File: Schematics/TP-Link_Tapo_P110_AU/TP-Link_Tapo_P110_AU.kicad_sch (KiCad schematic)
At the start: 28 parts, among them J1 KB-6160 Daughterboard, Q2 MMBT3904, Q3 MMBT3904, U1 SY22841, U7 BL0937

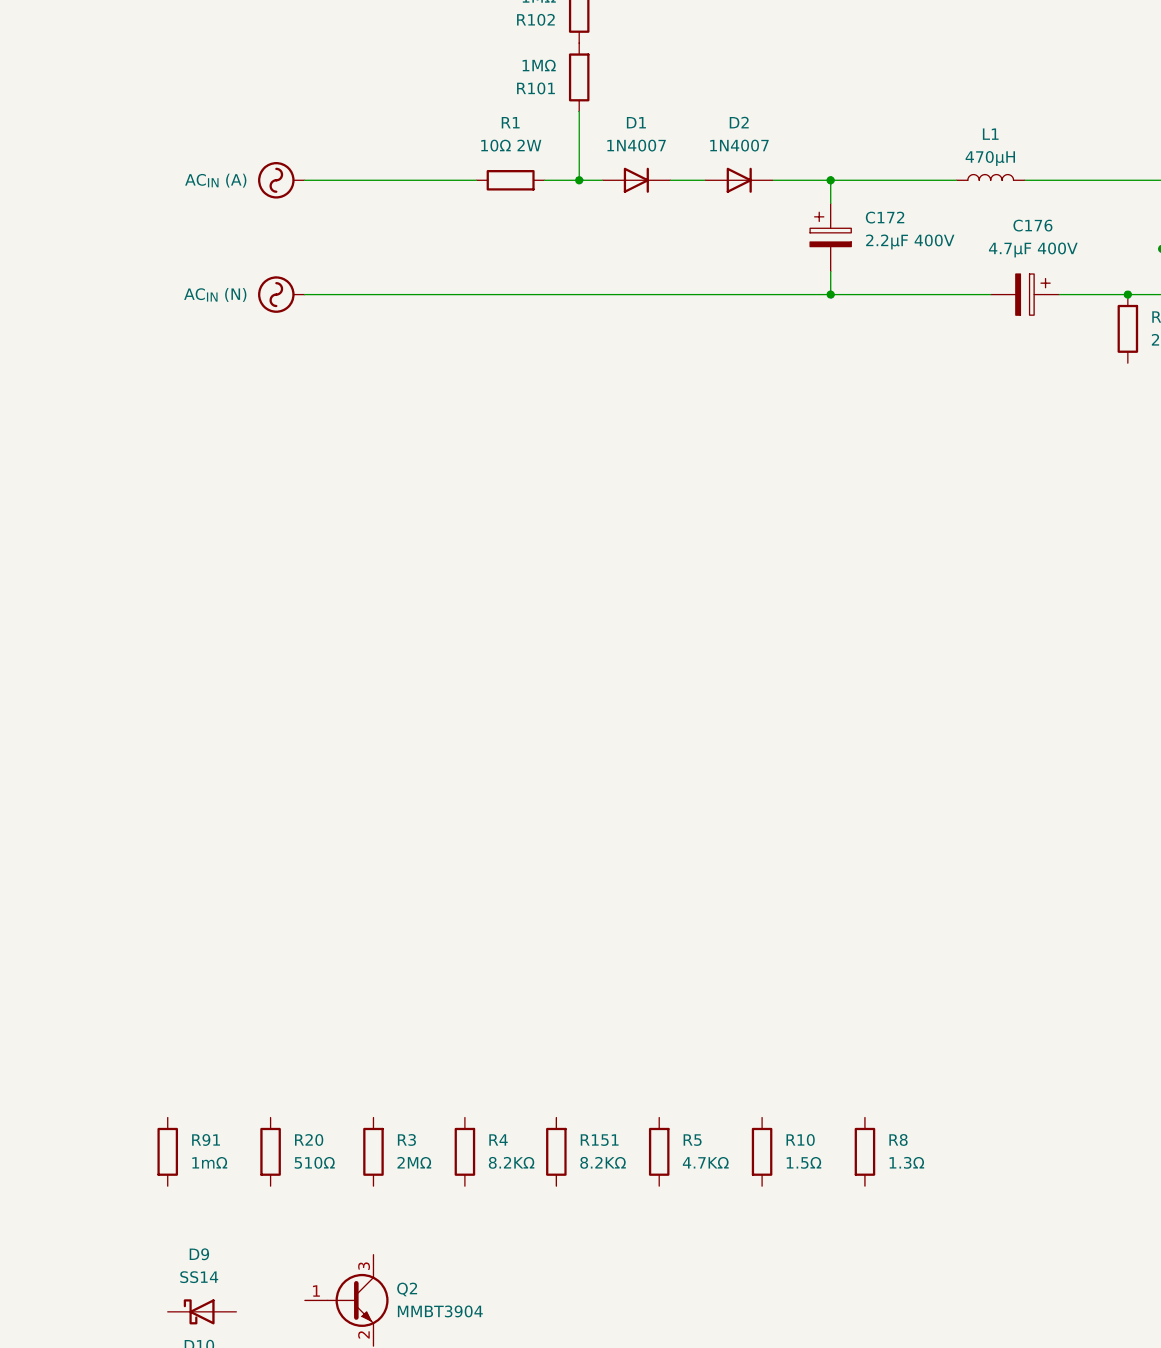
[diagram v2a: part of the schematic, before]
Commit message: Added more components
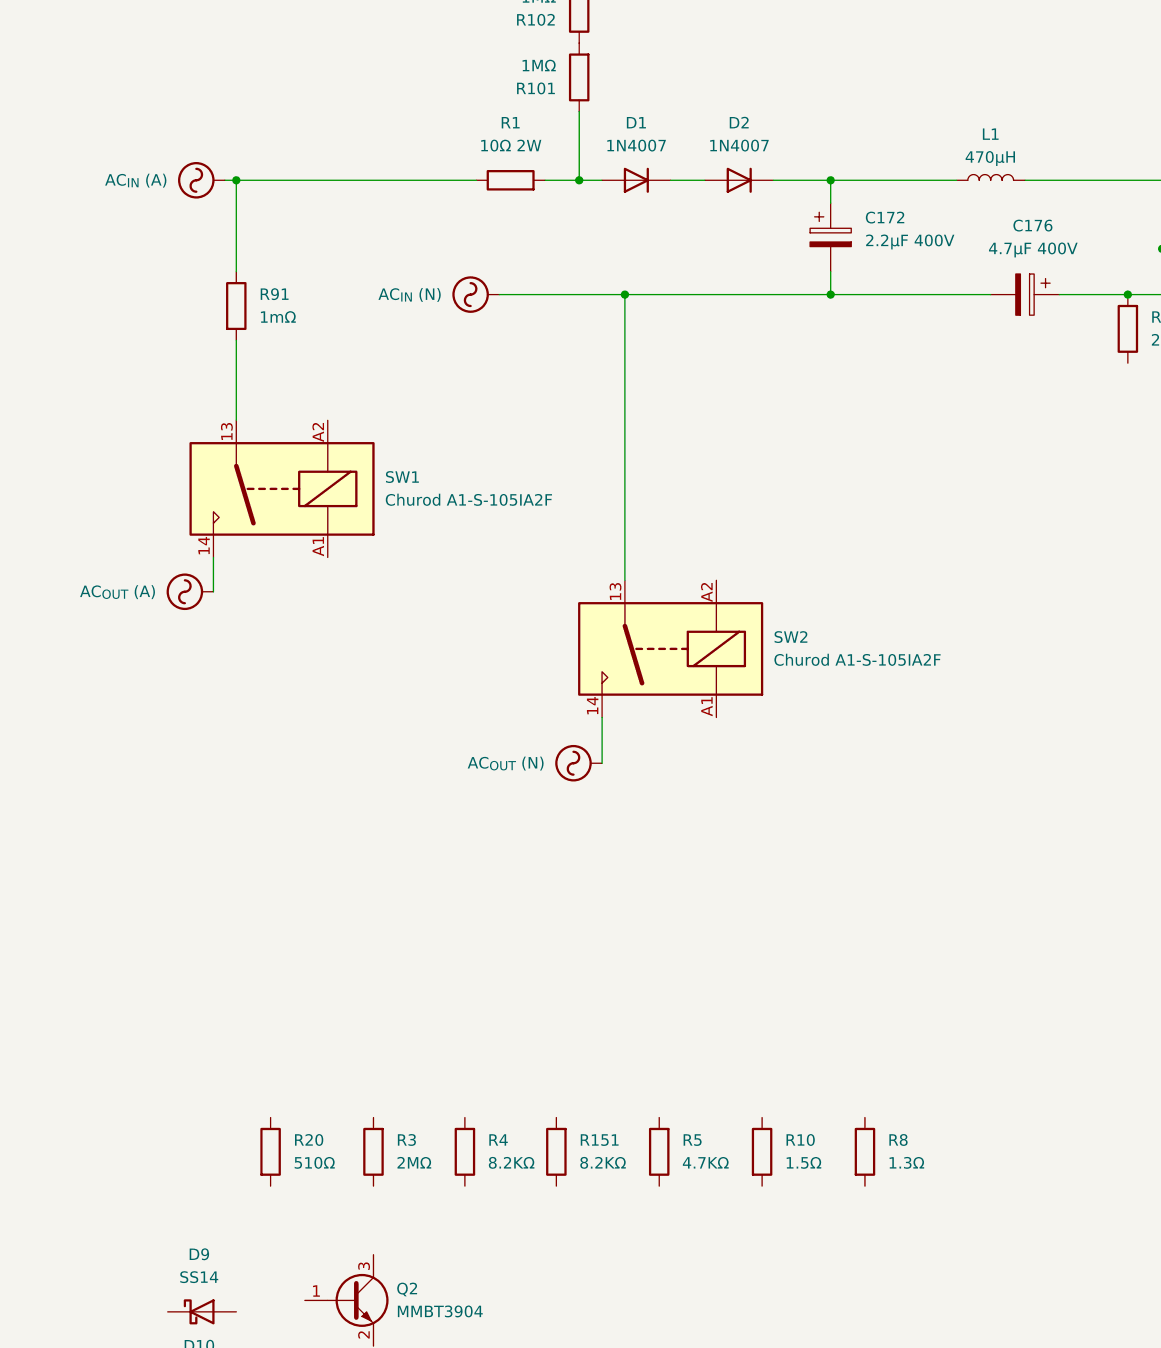
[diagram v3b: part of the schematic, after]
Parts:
- added SW1, SW2: Churod A1-S-105IA2F, symbol Relay:Relay_SPST-NO
- D6: footprint (none) -> LED_THT:LED_D5.0mm-3
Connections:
- net AC_{IN} (A): now also R91.1
- net AC_{IN} (N): now also SW2.13
- net at R91.2: now also SW1.13
- new net AC_{OUT} (A): SW1.14
- new net AC_{OUT} (N): SW2.14
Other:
- moved on the sheet: R91
